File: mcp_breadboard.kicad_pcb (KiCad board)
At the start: 2 copper layers, 53.3 x 35.6 mm, 33 parts, among them J1 VDD, J2 VDD, J3 GPIO, J4 UART/SPI, J5 USB_B_Micro, SW1 SW_SPDT, SW2 RST, SW3 SW_DIP_x04, U1 MCP2221AxSL, U2 MCP1826S

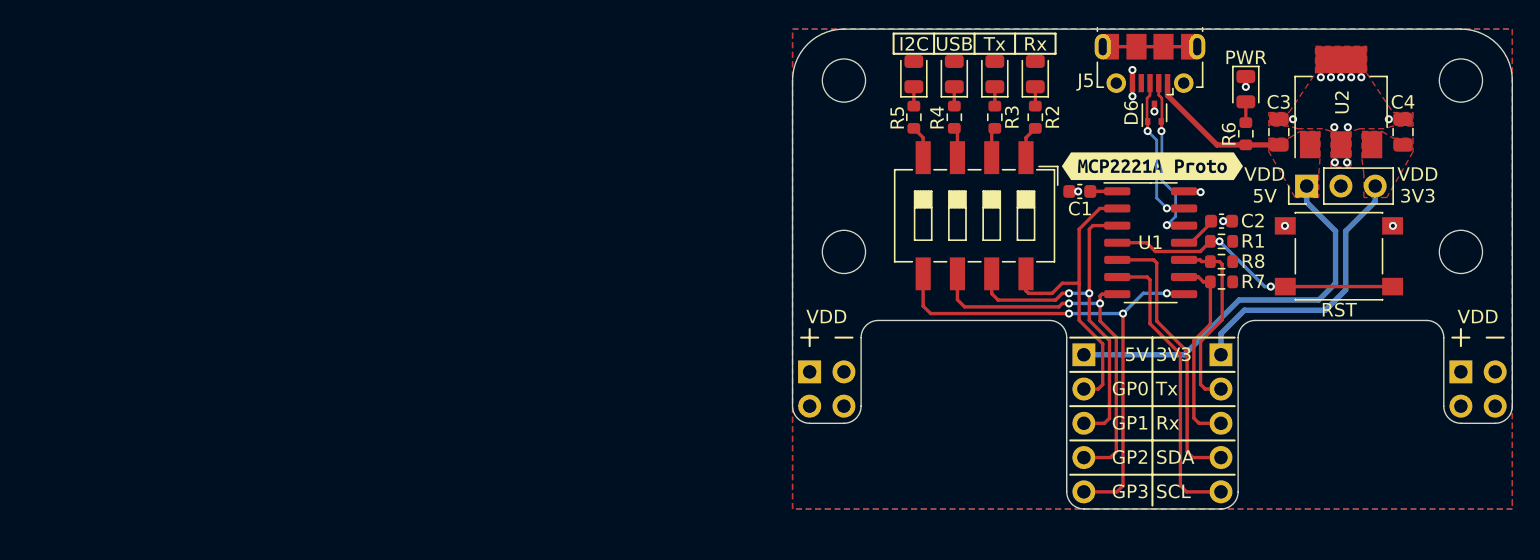
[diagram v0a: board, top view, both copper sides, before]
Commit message: Final rev of design and layout, metrification of major board features for easier laser cutting.
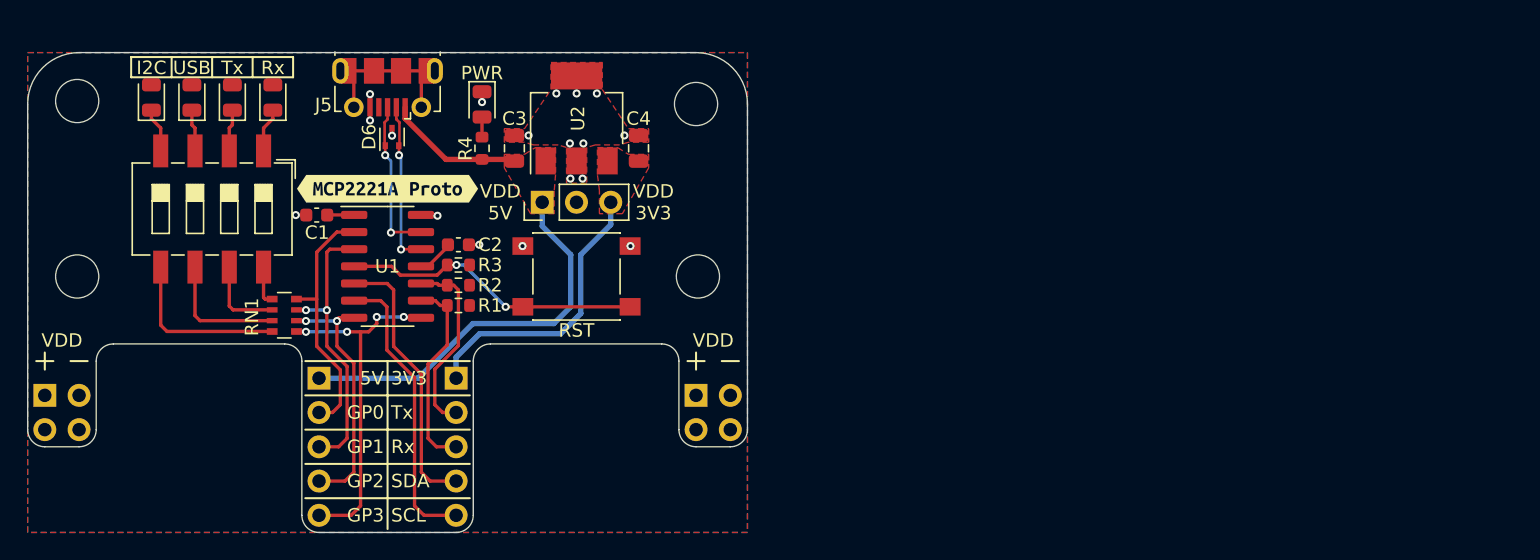
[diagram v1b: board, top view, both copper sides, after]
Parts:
- removed the R2 at (98.0, 33.2)
- removed the R3 at (95.0, 33.2)
- removed the R4 at (92.0, 33.2)
- removed R5: 1k, Resistor_SMD:R_0603_1608Metric
- added RN1: 1k, Resistor_SMD:R_Array_Convex_4x0603, F.Cu at (42.4, 47.9)
- SW3: renamed from SW1; value SW_SPDT -> VDD_SEL
- moved H1 56.8 mm to (27.0, 45.0)
- moved H2 56.8 mm to (27.0, 32.0)
- moved J4 56.7 mm to (55.1, 52.5)
- moved J1 56.7 mm to (24.6, 53.8)
- moved H3 56.7 mm to (72.9, 32.2)
- moved J2 56.7 mm to (72.9, 53.8)
- moved J3 56.7 mm to (44.9, 52.5)
- moved kibuzzard-627C3F81 56.7 mm to (50.0, 38.5)
- moved C4 56.7 mm to (68.6, 35.5)
- moved C3 56.7 mm to (59.4, 35.5)
- moved SW3 56.7 mm to (61.5, 39.5)
- moved U2 56.7 mm to (64.0, 33.3)
- moved D5 56.6 mm to (57.0, 32.2)
- moved R4 56.6 mm to (57.0, 35.5)
- moved C1 56.6 mm to (44.8, 40.5)
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- renumbered R7 to R1, R8 to R2, R1 to R3, R6 to R4, SW2 to SW1, SW3 to SW2
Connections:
- SW2 pad 1: Net-(R2-Pad2) -> Net-(D1-Pad1)
- SW2 pad 2: Net-(R3-Pad2) -> Net-(D2-Pad1)
- SW2 pad 3: Net-(R4-Pad1) -> Net-(D3-Pad1)
- SW2 pad 4: Net-(R5-Pad2) -> Net-(D4-Pad1)
- SW2 pad 5: G3 -> Net-(RN1-Pad4)
- SW2 pad 6: G2 -> Net-(RN1-Pad3)
- SW2 pad 7: G1 -> Net-(RN1-Pad2)
- SW2 pad 8: G0 -> Net-(RN1-Pad1)
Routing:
- net Net-(RN1-Pad4): track 0.00 -> 12.8 mm
- net G3: track 38.4 -> 26.3 mm, vias 3 -> 4
- net G2: track 28.8 -> 19.0 mm
- net Net-(RN1-Pad3): track 0.00 -> 9.47 mm
- net G1: track 28.0 -> 21.1 mm
- net Net-(RN1-Pad2): track 0.00 -> 6.18 mm
- net unconnected-(J5-Pad6): track 6.40 -> 12.1 mm
- net G0: track 22.8 -> 18.7 mm
- net Net-(RN1-Pad1): track 0.00 -> 2.94 mm
- net Net-(R5-Pad2): track 2.46 -> 0.00 mm
- net Net-(R2-Pad2): track 2.46 -> 0.00 mm
- net Net-(R4-Pad1): track 2.27 -> 0.00 mm
- net Net-(R3-Pad2): track 2.27 -> 0.00 mm
- net Net-(D4-Pad1): track 1.44 -> 3.30 mm
- net Net-(D1-Pad1): track 1.44 -> 3.30 mm
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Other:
- outline, holes or cut-outs redrawn
- board text added: "MCP2221A Prototyping Board Rev1 Thomas Bytheway ghub:HarkonenBade/MCP2221a-proto 2022-05-14"

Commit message: Final tweaks
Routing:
- net unconnected-(J5-Pad6): track 12.1 -> 13.8 mm
- net GND: track 6.09 -> 5.12 mm, vias 18 -> 22
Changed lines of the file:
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@@
     (descr "Capacitor SMD 0805 (2012 Metric), square (rectangular) end terminal, IPC_7351 nominal, (Body size source: IPC-SM-782 page 76, https://www.pcb-3d.com/wordpress/wp-content/uploads/ipc-sm-782a_amendment_1_and_2.pdf, https://docs.google.com/spreadsheets/d/1BsfQQcO9C6DZCsRaXUlFlo91Tg2WpOkGARC1WS5S8t0/edit?usp=sharing), generated with kicad-footprint-generator")
     (tags "capacitor")
+    (property "LCSC" "C1713")
     (property "Sheetfile" "mcp_breadboard.kicad_sch")
     (property "Sheetname" "")
@@
     (descr "Capacitor SMD 0805 (2012 Metric), square (rectangular) end terminal, IPC_7351 nominal, (Body size source: IPC-SM-782 page 76, https://www.pcb-3d.com/wordpress/wp-content/uploads/ipc-sm-782a_amendment_1_and_2.pdf, https://docs.google.com/spreadsheets/d/1BsfQQcO9C6DZCsRaXUlFlo91Tg2WpOkGARC1WS5S8t0/edit?usp=sharing), generated with kicad-footprint-generator")
     (tags "capacitor")
+    (property "LCSC" "C1713")
     (property "Sheetfile" "mcp_breadboard.kicad_sch")
     (property "Sheetname" "")
@@
     (descr "SOT523, https://www.diodes.com/assets/Package-Files/SOT523.pdf")
     (tags "SOT-523")
+    (property "LCSC" "C117553")
     (property "Sheetfile" "mcp_breadboard.kicad_sch")
     (property "Sheetname" "")
@@
     (descr "tactile push button, 6x6mm e.g. PTS645xx series, height=9.5mm")
     (tags "tact sw push 6mm smd")
+    (property "LCSC" "C493020")
     (property "Sheetfile" "mcp_breadboard.kicad_sch")
     (property "Sheetname" "")
@@
     (descr "SMD 4x-dip-switch SPST , Slide, row spacing 8.61 mm (338 mils), body size 6.7x11.72mm (see e.g. https://www.ctscorp.com/wp-content/uploads/219.pdf), SMD, LowProfile")
     (tags "SMD DIP Switch SPST Slide 8.61mm 338mil SMD LowProfile")
+    (property "LCSC" "C437204")
     (property "Sheetfile" "mcp_breadboard.kicad_sch")
     (property "Sheetname" "")
@@
     (descr "Chip Resistor Network, ROHM MNR14 (see mnr_g.pdf)")
     (tags "resistor array")
+    (property "LCSC" "C425239")
     (property "Sheetfile" "mcp_breadboard.kicad_sch")
     (property "Sheetname" "")
@@
   (segment (start 63.57 43.39) (end 63.57 47.24) (width 0.4) (layer "B.Cu") (net 1))
   (segment (start 52.27 52.54) (end 44.92 52.54) (width 0.4) (layer "B.Cu") (net 1))
-  (segment (start 48.7 32.4625) (end 48.7 31.49) (width 0.25) (layer "F.Cu") (net 2))
   (segment (start 48.7 33.44) (end 48.7 32.4625) (width 0.25) (layer "F.Cu") (net 2))
   (segment (start 50.331 34.012351) (end 50.331 34.5895) (width 0.25) (layer "F.Cu") (net 2))
@@
   (via (at 60 42.75) (size 0.6) (drill 0.3) (layers "F.Cu" "B.Cu") (net 2))
   (via (at 48.7 33.44) (size 0.6) (drill 0.3) (layers "F.Cu" "B.Cu") (net 2))
-  (via (at 48.7 31.49) (size 0.6) (drill 0.3) (layers "F.Cu" "B.Cu") (net 2))
   (via (at 53.7 40.5) (size 0.6) (drill 0.3) (layers "F.Cu" "B.Cu") (net 2))
+  (via (at 65.6 30.85) (size 0.6) (drill 0.3) (layers "F.Cu" "B.Cu") (net 2))
+  (via (at 58.35 34.55) (size 0.6) (drill 0.3) (layers "F.Cu" "B.Cu") (free) (net 2))
+  (via (at 69.65 34.55) (size 0.6) (drill 0.3) (layers "F.Cu" "B.Cu") (free) (net 2))
   (via (at 57 32.077) (size 0.6) (drill 0.3) (layers "F.Cu" "B.Cu") (net 2))
-  (via (at 64.01 31.44) (size 0.6) (drill 0.3) (layers "F.Cu" "B.Cu") (free) (net 2))
+  (via (at 62.4 29.45) (size 0.6) (drill 0.3) (layers "F.Cu" "B.Cu") (free) (net 2))
   (via (at 63.51 35.14) (size 0.6) (drill 0.3) (layers "F.Cu" "B.Cu") (free) (net 2))
   (via (at 56.8 42.65) (size 0.6) (drill 0.3) (layers "F.Cu" "B.Cu") (net 2))
   (via (at 43.2 40.45) (size 0.6) (drill 0.3) (layers "F.Cu" "B.Cu") (net 2))
   (via (at 63.55 37.75) (size 0.6) (drill 0.3) (layers "F.Cu" "B.Cu") (free) (net 2))
-  (via (at 62.51 31.44) (size 0.6) (drill 0.3) (layers "F.Cu" "B.Cu") (free) (net 2))
+  (via (at 62.4 30.85) (size 0.6) (drill 0.3) (layers "F.Cu" "B.Cu") (free) (net 2))
+  (via (at 64 29.45) (size 0.6) (drill 0.3) (layers "F.Cu" "B.Cu") (net 2))
   (via (at 68 42.75) (size 0.6) (drill 0.3) (layers "F.Cu" "B.Cu") (net 2))
   (via (at 60.45 34.55) (size 0.6) (drill 0.3) (layers "F.Cu" "B.Cu") (free) (net 2))
-  (via (at 65.51 31.44) (size 0.6) (drill 0.3) (layers "F.Cu" "B.Cu") (free) (net 2))
+  (via (at 65.6 29.45) (size 0.6) (drill 0.3) (layers "F.Cu" "B.Cu") (free) (net 2))
   (via (at 50.3305 34.565) (size 0.6) (drill 0.3) (layers "F.Cu" "B.Cu") (net 2))
+  (via (at 64 30.85) (size 0.6) (drill 0.3) (layers "F.Cu" "B.Cu") (net 2))
   (segment (start 64.32 43.39) (end 64.32 47.74) (width 0.4) (layer "B.Cu") (net 3))
   (segment (start 66.54 39.5) (end 66.54 41.16) (width 0.4) (layer "B.Cu") (net 3))
@@
   (segment (start 47.1 29.7625) (end 53.5 29.7625) (width 0.25) (layer "F.Cu") (net 23))
   (segment (start 47.5 30.1625) (end 47.1 29.7625) (width 0.25) (layer "F.Cu") (net 23))
-  (segment (start 52.5 32.4625) (end 52.5 30.1625) (width 0.25) (layer "F.Cu") (net 23))
-  (segment (start 47.5 32.4625) (end 47.5 30.1625) (width 0.25) (layer "F.Cu") (net 23))
+  (segment (start 53.5 31.4625) (end 53.5 29.7625) (width 0.25) (layer "B.Cu") (net 23))
+  (segment (start 47.5 32.4625) (end 46.5 31.4625) (width 0.25) (layer "B.Cu") (net 23))
+  (segment (start 52.5 32.4625) (end 53.5 31.4625) (width 0.25) (layer "B.Cu") (net 23))
+  (segment (start 46.5 31.4625) (end 46.5 29.7625) (width 0.25) (layer "B.Cu") (net 23))
   (segment (start 40.925 46.675) (end 40.81 46.56) (width 0.25) (layer "F.Cu") (net 24))
   (segment (start 40.81 46.56) (end 40.81 44.305) (width 0.25) (layer "F.Cu") (net 24))
@@
     (polygon
       (pts
-        (xy 65.91 29.14)
-        (xy 65.91 31.14)
         (xy 67.85 34.05)
-        (xy 69.35 34.05)
-        (xy 69.35 35.05)
+        (xy 69.95 34.05)
+        (xy 69.95 35.05)
         (xy 67.85 35.05)
         (xy 67.2 35.25)
@@
         (xy 60.8 35.25)
         (xy 60.15 35.05)
-        (xy 58.65 35.05)
-        (xy 58.65 34.05)
+        (xy 58.05 35.05)
+        (xy 58.05 34.05)
         (xy 60.15 34.05)
-        (xy 62.11 31.14)
-        (xy 62.11 29.14)
       )
     )

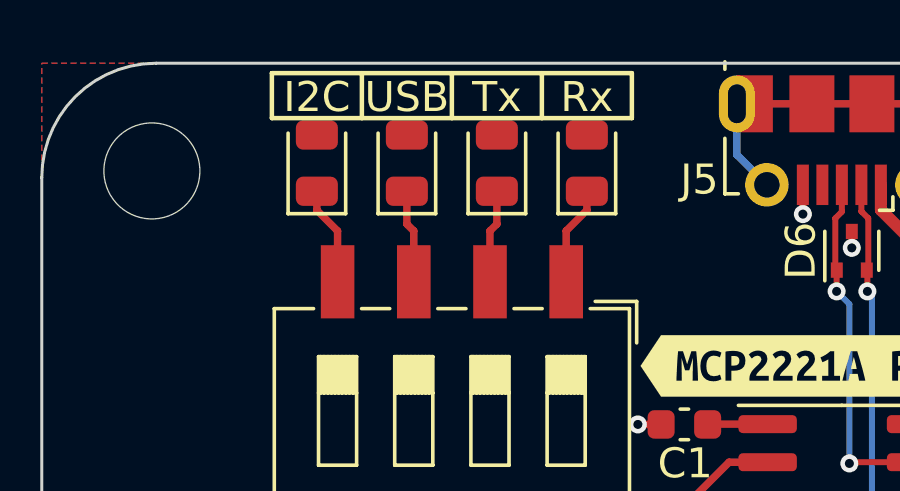
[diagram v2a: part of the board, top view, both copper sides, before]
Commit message: LEDs Moved around
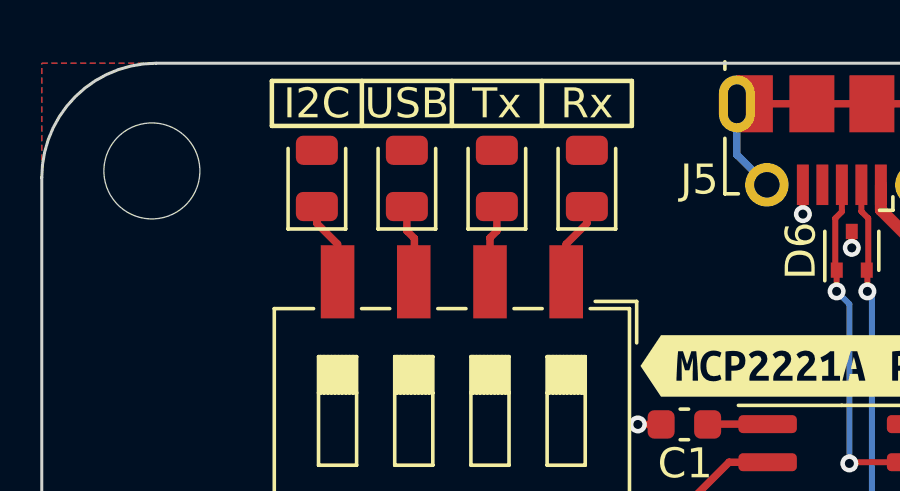
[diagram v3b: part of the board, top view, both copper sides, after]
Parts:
- moved D1 0.51 mm to (41.5, 32.2)
- moved D2 0.51 mm to (38.5, 32.2)
- moved D3 0.51 mm to (35.5, 32.2)
- moved D4 0.51 mm to (32.5, 32.2)
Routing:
- net Net-(D4-Pad1): track 3.30 -> 2.79 mm
- net Net-(D2-Pad1): track 3.11 -> 2.60 mm
- net Net-(D1-Pad1): track 3.30 -> 2.79 mm
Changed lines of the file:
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@@
   )
   (footprint "LED_SMD:LED_0805_2012Metric" (layer "F.Cu")
-    (at 35.5 31.74 90)
+    (at 35.5 32.25 90)
     (descr "LED SMD 0805 (2012 Metric), square (rectangular) end terminal, IPC_7351 nominal, (Body size source: https://docs.google.com/spreadsheets/d/1BsfQQcO9C6DZCsRaXUlFlo91Tg2WpOkGARC1WS5S8t0/edit?usp=sharing), generated with kicad-footprint-generator")
     (tags "LED")
@@
       (effects (font (size 1 1) (thickness 0.15)))
     )
-    (fp_text value "USB" (at 2.2 0) (layer "F.SilkS")
+    (fp_text value "USB" (at 2.5 0) (layer "F.SilkS")
       (effects (font (size 1 1) (thickness 0.15)))
     )
@@
   )
   (footprint "LED_SMD:LED_0805_2012Metric" (layer "F.Cu")
-    (at 32.5 31.74 90)
+    (at 32.5 32.25 90)
     (descr "LED SMD 0805 (2012 Metric), square (rectangular) end terminal, IPC_7351 nominal, (Body size source: https://docs.google.com/spreadsheets/d/1BsfQQcO9C6DZCsRaXUlFlo91Tg2WpOkGARC1WS5S8t0/edit?usp=sharing), generated with kicad-footprint-generator")
     (tags "LED")
@@
       (effects (font (size 1 1) (thickness 0.15)))
     )
-    (fp_text value "I2C" (at 2.2 0) (layer "F.SilkS")
+    (fp_text value "I2C" (at 2.5 0) (layer "F.SilkS")
       (effects (font (size 1 1) (thickness 0.15)))
     )
@@
   )
   (footprint "LED_SMD:LED_0805_2012Metric" (layer "F.Cu")
-    (at 41.5 31.74 90)
+    (at 41.5 32.25 90)
     (descr "LED SMD 0805 (2012 Metric), square (rectangular) end terminal, IPC_7351 nominal, (Body size source: https://docs.google.com/spreadsheets/d/1BsfQQcO9C6DZCsRaXUlFlo91Tg2WpOkGARC1WS5S8t0/edit?usp=sharing), generated with kicad-footprint-generator")
     (tags "LED")
@@
       (effects (font (size 1 1) (thickness 0.15)))
     )
-    (fp_text value "Rx" (at 2.2 0) (layer "F.SilkS")
+    (fp_text value "Rx" (at 2.5 0) (layer "F.SilkS")
       (effects (font (size 1 1) (thickness 0.15)))
     )
@@
   )
   (footprint "LED_SMD:LED_0805_2012Metric" (layer "F.Cu")
-    (at 38.5 31.74 90)
+    (at 38.5 32.25 90)
     (descr "LED SMD 0805 (2012 Metric), square (rectangular) end terminal, IPC_7351 nominal, (Body size source: https://docs.google.com/spreadsheets/d/1BsfQQcO9C6DZCsRaXUlFlo91Tg2WpOkGARC1WS5S8t0/edit?usp=sharing), generated with kicad-footprint-generator")
     (tags "LED")
@@
       (effects (font (size 1 1) (thickness 0.15)))
     )
-    (fp_text value "Tx" (at 2.2 0) (layer "F.SilkS")
+    (fp_text value "Tx" (at 2.5 0) (layer "F.SilkS")
       (effects (font (size 1 1) (thickness 0.15)))
     )
@@
   )
   (gr_line (start 50 51.27) (end 43.904 51.27) (layer "F.SilkS") (width 0.15))
-  (gr_line (start 40 28.74) (end 40 30.24) (layer "F.SilkS") (width 0.15))
+  (gr_line (start 40 29) (end 40 30.5) (layer "F.SilkS") (width 0.15))
   (gr_line (start 43.904 58.89) (end 50 58.89) (layer "F.SilkS") (width 0.15))
   (gr_line (start 50 63.716) (end 50 51.27) (layer "F.SilkS") (width 0.15))
   (gr_line (start 74.765 51.27) (end 76.035 51.27) (layer "F.SilkS") (width 0.15))
   (gr_line (start 72.86 51.905) (end 72.86 50.635) (layer "F.SilkS") (width 0.15))
-  (gr_line (start 31 30.24) (end 43 30.24) (layer "F.SilkS") (width 0.15))
+  (gr_line (start 31 30.5) (end 43 30.5) (layer "F.SilkS") (width 0.15))
   (gr_line (start 56.096 53.81) (end 50 53.81) (layer "F.SilkS") (width 0.15))
-  (gr_line (start 34 28.74) (end 34 30.24) (layer "F.SilkS") (width 0.15))
+  (gr_line (start 34 29) (end 34 30.5) (layer "F.SilkS") (width 0.15))
   (gr_line (start 56.096 61.43) (end 50 61.43) (layer "F.SilkS") (width 0.15))
   (gr_line (start 26.505 51.27) (end 27.775 51.27) (layer "F.SilkS") (width 0.15))
@@
   (gr_line (start 50 53.81) (end 43.904 53.81) (layer "F.SilkS") (width 0.15))
   (gr_line (start 50 56.35) (end 43.904 56.35) (layer "F.SilkS") (width 0.15))
-  (gr_line (start 43 28.74) (end 43 30.24) (layer "F.SilkS") (width 0.15))
+  (gr_line (start 43 29) (end 43 30.5) (layer "F.SilkS") (width 0.15))
   (gr_line (start 24.6 50.635) (end 24.6 51.905) (layer "F.SilkS") (width 0.15))
   (gr_line (start 43.904 61.43) (end 50 61.43) (layer "F.SilkS") (width 0.15))
@@
   (gr_line (start 73.495 51.27) (end 72.225 51.27) (layer "F.SilkS") (width 0.15))
   (gr_line (start 56.096 58.89) (end 50 58.89) (layer "F.SilkS") (width 0.15))
-  (gr_line (start 43 28.74) (end 31 28.74) (layer "F.SilkS") (width 0.15))
+  (gr_line (start 43 29) (end 31 29) (layer "F.SilkS") (width 0.15))
   (gr_line (start 56.096 56.35) (end 50 56.35) (layer "F.SilkS") (width 0.15))
-  (gr_line (start 31 28.74) (end 31 30.24) (layer "F.SilkS") (width 0.15))
-  (gr_line (start 37 28.74) (end 37 30.24) (layer "F.SilkS") (width 0.15))
+  (gr_line (start 31 29) (end 31 30.5) (layer "F.SilkS") (width 0.15))
+  (gr_line (start 37 29) (end 37 30.5) (layer "F.SilkS") (width 0.15))
   (gr_arc (start 24.6 57.62) (mid 23.701974 57.248026) (end 23.33 56.35) (layer "Edge.Cuts") (width 0.1))
   (gr_line (start 23.33 32.22) (end 23.33 56.35) (layer "Edge.Cuts") (width 0.1))
@@
   (segment (start 53 44.25) (end 54.475 42.775) (width 0.25) (layer "F.Cu") (net 5))
   (segment (start 52.475 44.25) (end 53 44.25) (width 0.25) (layer "F.Cu") (net 5))
-  (segment (start 41.5 33.31) (end 41.5 32.6775) (width 0.25) (layer "F.Cu") (net 6))
-  (segment (start 40.81 35.695) (end 40.81 34) (width 0.25) (layer "F.Cu") (net 6))
-  (segment (start 40.81 34) (end 41.5 33.31) (width 0.25) (layer "F.Cu") (net 6))
-  (segment (start 38.27 34) (end 38.5 33.77) (width 0.25) (layer "F.Cu") (net 7))
-  (segment (start 38.27 35.695) (end 38.27 34) (width 0.25) (layer "F.Cu") (net 7))
-  (segment (start 38.5 33.77) (end 38.5 32.6775) (width 0.25) (layer "F.Cu") (net 7))
-  (segment (start 35.73 34) (end 35.5 33.77) (width 0.25) (layer "F.Cu") (net 8))
-  (segment (start 35.5 33.77) (end 35.5 32.6775) (width 0.25) (layer "F.Cu") (net 8))
-  (segment (start 35.73 35.695) (end 35.73 34) (width 0.25) (layer "F.Cu") (net 8))
-  (segment (start 33.19 34) (end 32.5 33.31) (width 0.25) (layer "F.Cu") (net 9))
-  (segment (start 32.5 33.31) (end 32.5 32.6775) (width 0.25) (layer "F.Cu") (net 9))
-  (segment (start 33.19 35.695) (end 33.19 34) (width 0.25) (layer "F.Cu") (net 9))
+  (segment (start 41.5 33.75) (end 41.5 33.1875) (width 0.25) (layer "F.Cu") (net 6))
+  (segment (start 40.81 35.695) (end 40.81 34.44) (width 0.25) (layer "F.Cu") (net 6))
+  (segment (start 40.81 34.44) (end 41.5 33.75) (width 0.25) (layer "F.Cu") (net 6))
+  (segment (start 38.5 34) (end 38.5 33.1875) (width 0.25) (layer "F.Cu") (net 7))
+  (segment (start 38.27 34.23) (end 38.5 34) (width 0.25) (layer "F.Cu") (net 7))
+  (segment (start 38.27 35.695) (end 38.27 34.23) (width 0.25) (layer "F.Cu") (net 7))
+  (segment (start 35.73 35.695) (end 35.75 35.675) (width 0.25) (layer "F.Cu") (net 8))
+  (segment (start 35.75 35.675) (end 35.75 34.25) (width 0.25) (layer "F.Cu") (net 8))
+  (segment (start 35.75 34.25) (end 35.5 34) (width 0.25) (layer "F.Cu") (net 8))
+  (segment (start 35.5 34) (end 35.5 33.1875) (width 0.25) (layer "F.Cu") (net 8))
+  (segment (start 33.19 35.695) (end 33.19 34.44) (width 0.25) (layer "F.Cu") (net 9))
+  (segment (start 32.5 33.75) (end 32.5 33.1875) (width 0.25) (layer "F.Cu") (net 9))
+  (segment (start 33.19 34.44) (end 32.5 33.75) (width 0.25) (layer "F.Cu") (net 9))
   (segment (start 57 34.675) (end 57 33.1355) (width 0.25) (layer "F.Cu") (net 10))
   (segment (start 46.5 54.5) (end 45.92 55.08) (width 0.25) (layer "F.Cu") (net 11))
